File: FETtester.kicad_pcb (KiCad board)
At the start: 2 copper layers, 68.6 x 53.3 mm, 80 parts, among them J1 Conn_01x06_Male, J2 Conn_02x03_Counter_Clockwise, Q1 MMSS8050, Q2 BF862, U1 LMC6044, U2 LMC6044, U3 LM324, U4 AD7249ARZ, U5 LM7705, U6 LDK320ADU120R

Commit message: Minor routing changes.
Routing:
- net +10V: track 112.7 -> 113.2 mm
- net GND: vias 104 -> 115

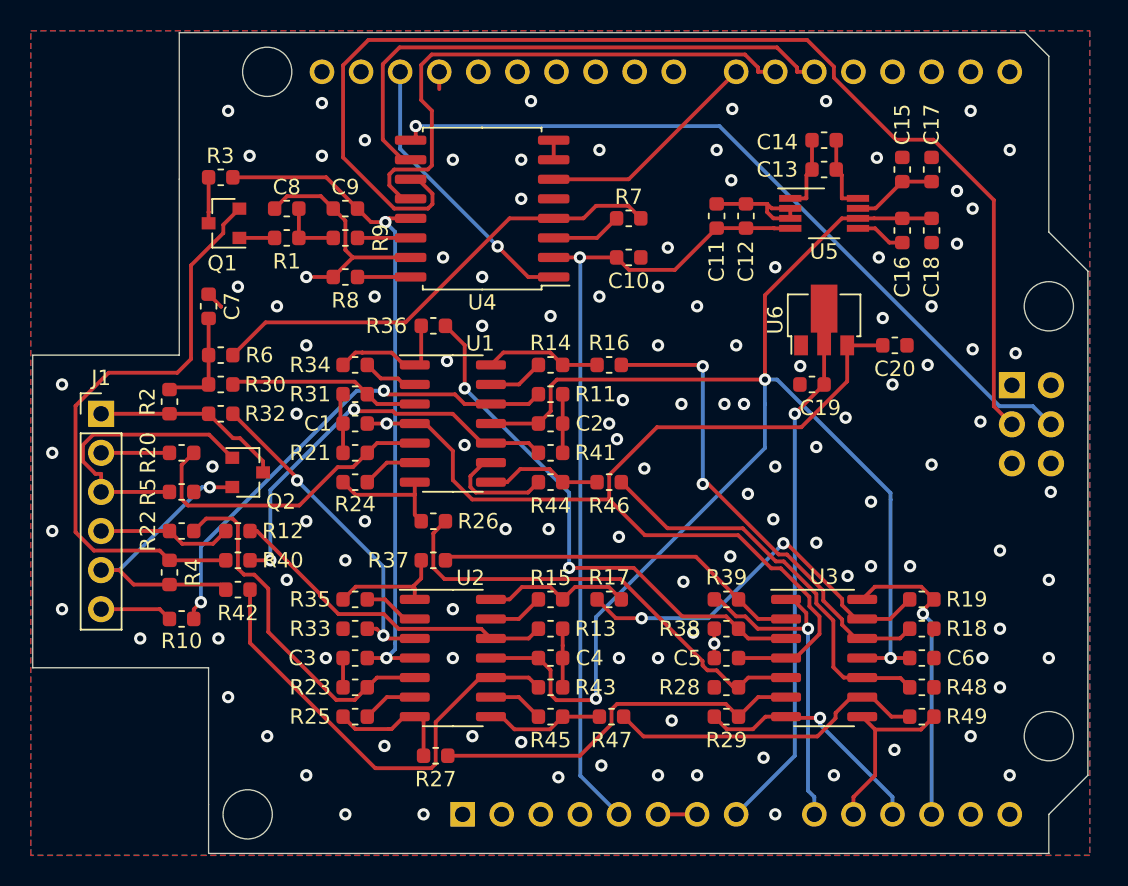
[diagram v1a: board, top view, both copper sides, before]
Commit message: Added negative swing on gate-source bias and RTD connection.
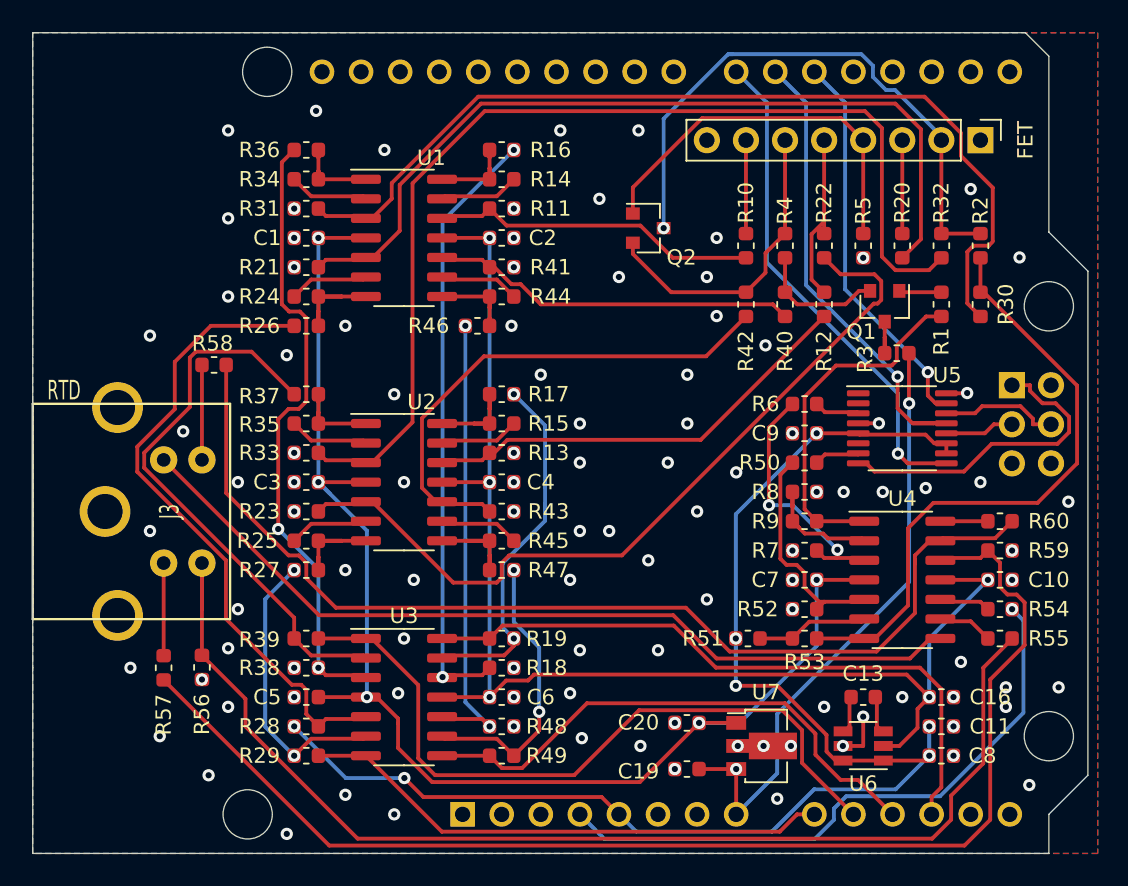
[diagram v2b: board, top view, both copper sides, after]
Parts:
- removed C12: 0.1uF, Capacitor_SMD:C_0603_1608Metric
- removed C14, C15: DNP, Capacitor_SMD:C_0603_1608Metric
- removed C17: 4.7uF, Capacitor_SMD:C_0603_1608Metric
- removed C18: 0.47uF, Capacitor_SMD:C_0603_1608Metric
- added J3: RTD, FETtester:DIN_4, F.Cu at (114.3, 104.8)
- added R50: 787, Resistor_SMD:R_0603_1608Metric, F.Cu at (164.5, 101.6)
- added R51: 12.4k, Resistor_SMD:R_0603_1608Metric, F.Cu at (160.8, 113.0)
- added R52: 10k, Resistor_SMD:R_0603_1608Metric, F.Cu at (164.5, 111.1)
- added R53: 10k, Resistor_SMD:R_0603_1608Metric, F.Cu at (164.5, 113.0)
- added R54: 10k, Resistor_SMD:R_0603_1608Metric, F.Cu at (177.2, 111.1)
- added R55: 10k, Resistor_SMD:R_0603_1608Metric, F.Cu at (177.2, 113.0)
- added R56: 3.32k, Resistor_SMD:R_0603_1608Metric, F.Cu at (125.3, 114.9)
- added R57: 339, Resistor_SMD:R_0603_1608Metric, F.Cu at (122.8, 114.9)
- added R58: 2.8k, Resistor_SMD:R_0603_1608Metric, F.Cu at (126.1, 95.2)
- added R59: 10k, Resistor_SMD:R_0603_1608Metric, F.Cu at (177.2, 107.3)
- added R60: 100k, Resistor_SMD:R_0603_1608Metric, F.Cu at (177.2, 105.4)
- added U7: L78L10, Package_TO_SOT_SMD:SOT-89-3, F.Cu at (161.7, 120.0)
- C11, C16: value 22uF -> 10uF
- C13: value 4.7uF -> 1uF
- C19, C20: value 1uF -> 10uF
- C8: value 0.1uF -> 10uF
- J1: value Conn_01x06_Male -> FET; footprint Connector_PinHeader_2.54mm:PinHeader_1x06_P2.54mm_Vertical -> Connector_PinHeader_2.54mm:PinHeader_1x08_P2.54mm_Vertical
- R10, R12, R14, R15, R16, R17, R18, R19, R20, R22, R24, R25, R28, R29, R30, R32, R34, R35, R36, R37, R38, R39, R40, R42, R44, R45, R46, R47, R48, R49: value 100k -> 10k
- R26: value 200k -> 6k
- R27: value 200k -> 30k
- R6, R8, R9: value 50 -> 10k
- R7: value 50 -> DNP
- U4: value AD7249ARZ -> LM324; footprint Package_SO:SOIC-16W_7.5x10.3mm_P1.27mm -> Package_SO:SOIC-14_3.9x8.7mm_P1.27mm
- U5: value LM7705 -> AD5687; footprint Package_SO:VSSOP-8_3.0x3.0mm_P0.65mm -> Package_SO:TSSOP-16_4.4x5mm_P0.65mm
- U6: value LDK320ADU120R -> LTC1983; footprint Package_TO_SOT_SMD:SOT-89-3 -> Package_TO_SOT_SMD:TSOT-23-6
- moved J1 59.9 mm to (175.9, 80.6), turned to 270 degrees
- moved C8 55.4 mm to (173.4, 120.7), turned to 0 degrees
- moved R2 53.7 mm to (175.9, 87.5), turned to 270 degrees
- moved R30 49.7 mm to (175.9, 91.3), turned to 90 degrees
- moved R20 48.7 mm to (170.8, 87.5), turned to 90 degrees
- moved R32 48.1 mm to (173.4, 87.5), turned to 90 degrees
- moved R5 47.1 mm to (168.3, 87.5), turned to 270 degrees
- moved R22 45.7 mm to (165.7, 87.5), turned to 90 degrees
- moved R3 45.4 mm to (170.5, 94.5)
- moved R4 45.3 mm to (163.2, 87.5), turned to 90 degrees
- moved R10 44.0 mm to (160.7, 87.5), turned to 90 degrees
- moved Q1 43.3 mm to (169.7, 91.4), turned to 270 degrees
- moved R1 42.8 mm to (173.4, 91.3), turned to 90 degrees
- moved C7 42.6 mm to (164.5, 109.2), turned to 0 degrees
- moved R12 40.8 mm to (165.7, 91.3), turned to 90 degrees
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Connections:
- A1 pad 10: /Id -> /Ig
- A1 pad 11: /Vgs -> /Id
- A1 pad 20: /LDAC* -> /RESET*
- A1 pad 22: /CLR* -> /LDAC*
- A1 pad 9: /Ig -> /Vgs
- C10 pad 1: +5V -> GND
- C10 pad 2: GND -> -5V
- C16 pad 1: VSS -> -5V
- C2 pad 2: VSS -> -5V
- C4 pad 2: VSS -> -5V
- C6 pad 2: VSS -> -5V
- C7 pad 1: /VRg -> GND
- C7 pad 2: GND -> +10V
- C8 pad 1: /DACVd -> +5V
- C9 pad 1: +10V -> GND
- C9 pad 2: GND -> +5V
- J1 pad 1: /Vg -> GND
- J1 pad 2: /VgSense -> /Vg
- J1 pad 3: /Vs -> /VgSense
- J1 pad 4: /VsSense -> /Vs
- J1 pad 5: /Vd -> /VsSense
- J1 pad 6: /VdSense -> /Vd
- R28 pad 2: GND -> +5V
- R3 pad 1: +10V -> VIN
- R6 pad 2: /VRg -> /DACA
- R7 pad 2: Net-(R7-Pad2) -> GND
- R8 pad 1: Net-(R8-Pad1) -> GND
- R8 pad 2: GND -> Net-(R8-Pad2)
- R9 pad 1: Net-(R9-Pad1) -> Net-(R8-Pad2)
- U1 pad 11: VSS -> -5V
- U2 pad 11: VSS -> -5V
- U3 pad 11: VSS -> -5V
- U4 pad 1: /AREF -> /DACVd
- U4 pad 10: /LDAC* -> Net-(R54-Pad1)
- U4 pad 11: /SCK -> -5V
- U4 pad 12: /SYNC* -> Net-(R57-Pad1)
- U4 pad 13: +10V -> Net-(R58-Pad1)
- U4 pad 14: Net-(R9-Pad1) -> /VRTD
- U4 pad 2: +5V -> Net-(R8-Pad2)
- U4 pad 3: Net-(R7-Pad2) -> Net-(R6-Pad1)
- U4 pad 4: Net-(R6-Pad1) -> +10V
- U4 pad 5: GND -> Net-(R50-Pad1)
- U4 pad 6: /CLR* -> Net-(R51-Pad2)
- U4 pad 7: GND -> /VRg
- U4 pad 8: GND -> Net-(J3-Pad1)
- U4 pad 9: /MOSI -> Net-(R55-Pad1)
- U5 pad 1: Net-(C13-Pad1) -> Net-(U5-Pad1)
- U5 pad 2: GND -> Net-(U5-Pad2)
- U5 pad 3: GND -> /DACA
- U5 pad 4: +5V -> GND
- U5 pad 5: GND -> +5V
- U5 pad 6: VSS -> Net-(U5-Pad6)
- U5 pad 7: Net-(C15-Pad1) -> /DACB
- U5 pad 8: Net-(C13-Pad2) -> /MISO
- U6 pad 1: GND -> +5V
- U6 pad 2: VIN -> -5V
- U6 pad 3: +10V -> Net-(C13-Pad1)
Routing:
- net VSS: track 97.7 -> 0.00 mm, vias 3 -> 0
- net -5V: track 0.00 -> 86.2 mm, vias 0 -> 5
- net Net-(R57-Pad1): track 0.00 -> 82.0 mm
- net Net-(J3-Pad4): track 0.00 -> 77.6 mm
- net /SCK: track 78.5 -> 4.50 mm
- net Net-(R58-Pad1): track 0.00 -> 70.2 mm
- net Net-(J3-Pad1): track 0.00 -> 56.4 mm
- net Net-(R30-Pad1): track 12.5 -> 61.6 mm
- net Net-(R32-Pad1): track 21.8 -> 68.8 mm, vias 2 -> 0
- net GND: track 51.2 -> 5.96 mm, vias 115 -> 106
- net /MOSI: track 50.4 -> 7.70 mm, vias 1 -> 0
- net +3V3: track 0.00 -> 40.4 mm, vias 0 -> 1
- net +5V: track 54.1 -> 93.0 mm, vias 1 -> 7
- net Net-(R20-Pad1): track 20.3 -> 55.3 mm
- net /VRg: track 6.97 -> 41.1 mm
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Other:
- outline, holes or cut-outs redrawn

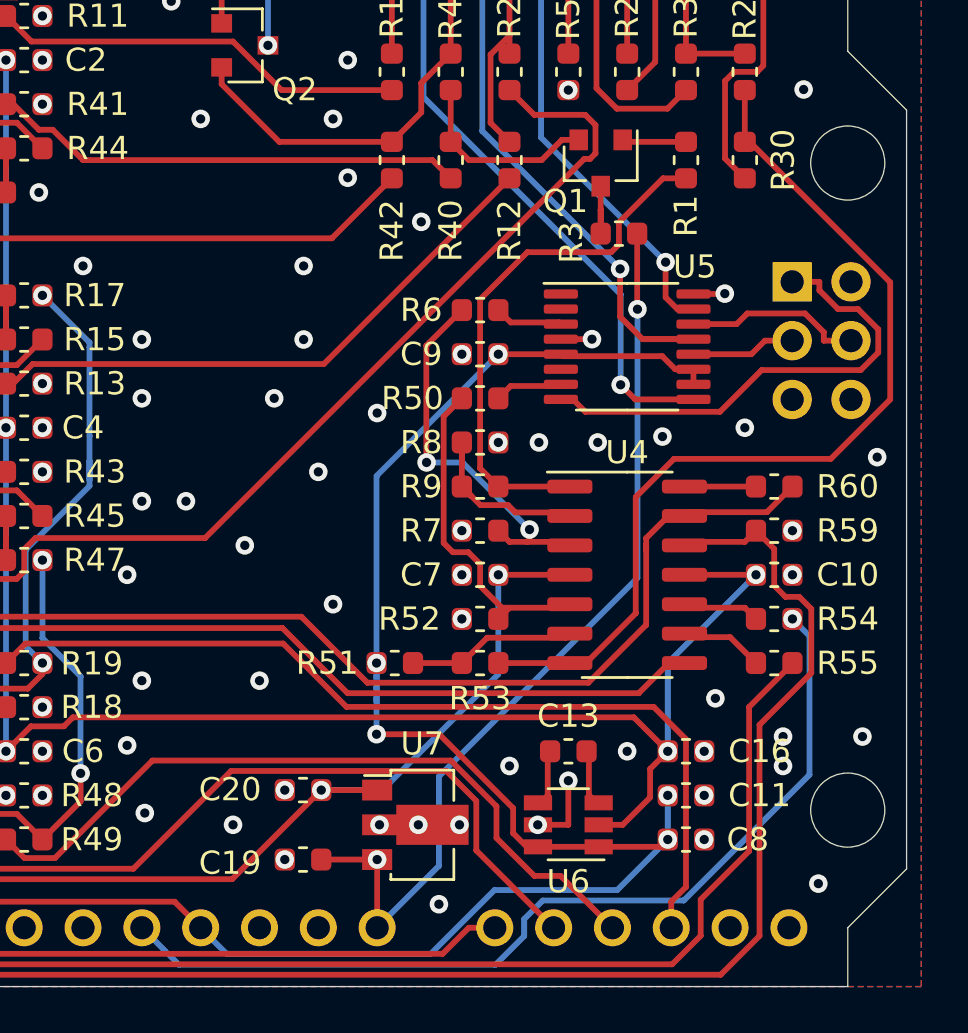
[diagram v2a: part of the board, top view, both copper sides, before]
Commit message: Fixed missing connection for RTD line.
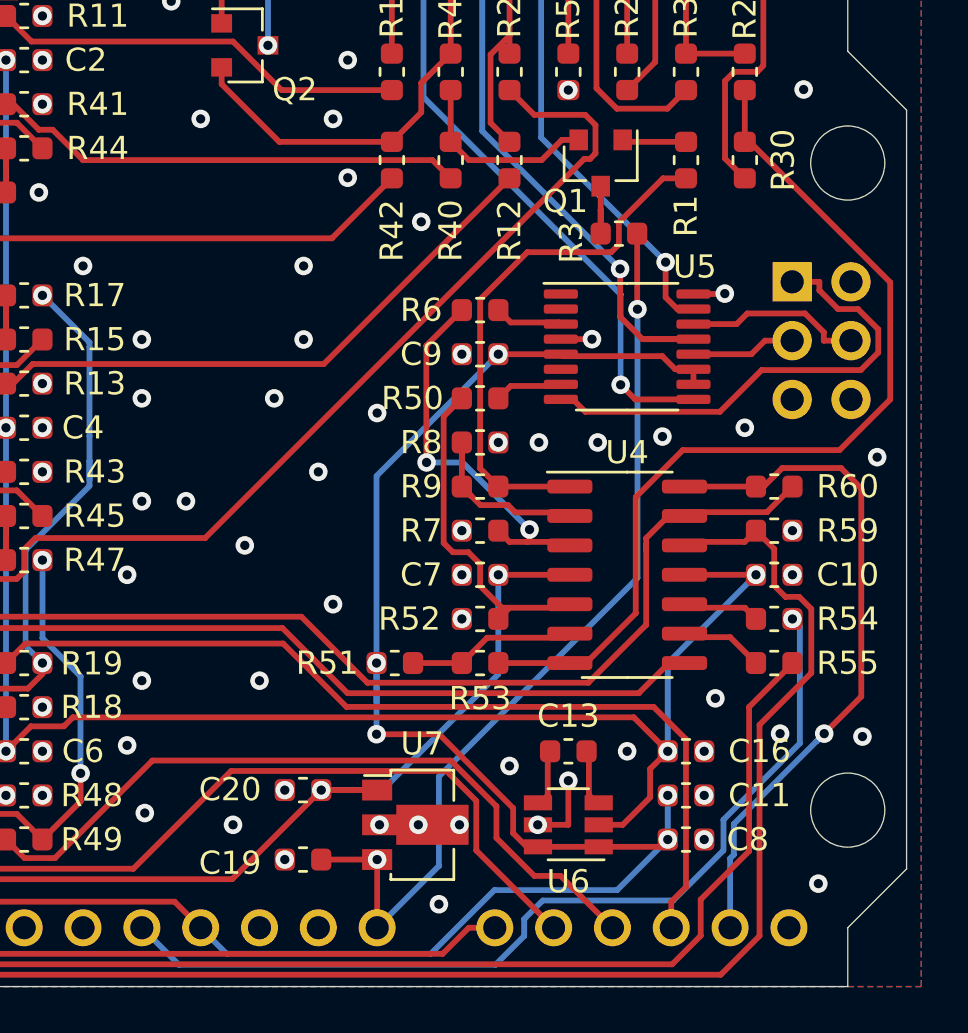
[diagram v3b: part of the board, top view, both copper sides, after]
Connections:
- A1 pad 13: Net-(A1-Pad13) -> /VRTD
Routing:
- net /VRTD: track 3.09 -> 29.6 mm, vias 0 -> 1
- net +3V3: track 40.4 -> 39.7 mm
- net GND: vias 106 -> 105
